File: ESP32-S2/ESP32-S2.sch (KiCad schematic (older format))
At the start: 45 parts, among them IC1 IP4220CZ6, J1 USB_A, J2 TYPE-C-31-M-12, J3 Conn_01x18_Male, J4 S2B-PH-SM4-TB(LF)(SN), J5 Conn_01x22_Male, SW1 SW_Push, SW2 SW_Push, U1 ESP32-S2-WROOM-ESP32-S2-WROOM, U2 MMBT8050, U3 MMBT8050, U4 MCP73831-2-OT, U5 AMS1117-3.3, U6 CH340C

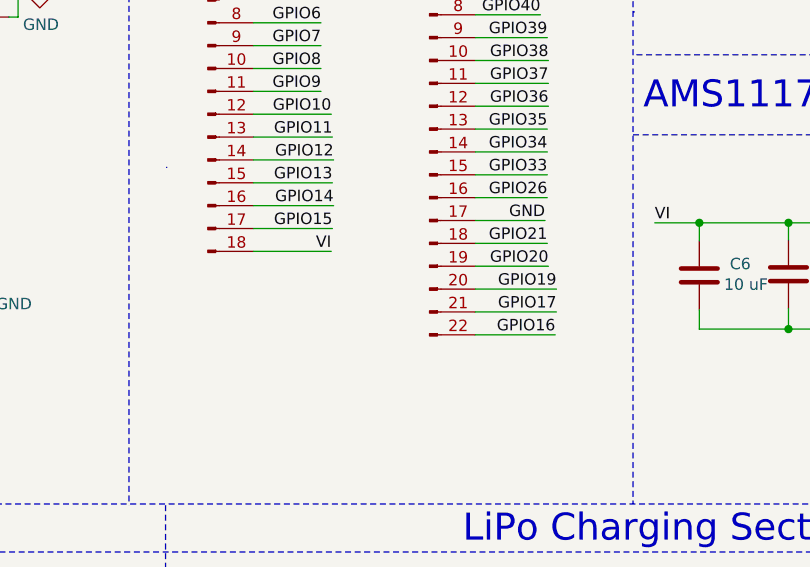
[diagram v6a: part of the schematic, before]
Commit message: Optimised 4-lyr routing v.4lyr.2
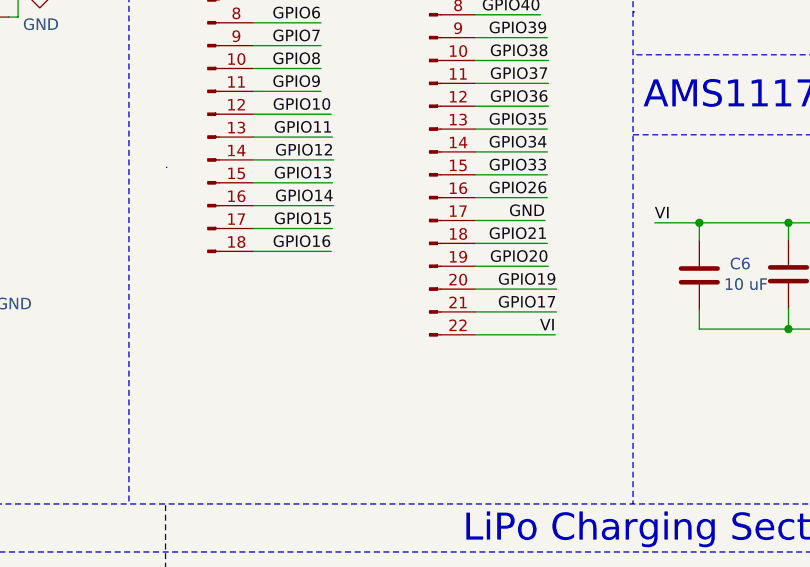
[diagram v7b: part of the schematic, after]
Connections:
- net GPIO16: now also J3.18 (Pin_18); no longer J5.22 (Pin_22)
- net VI: now also J5.22 (Pin_22); no longer J3.18 (Pin_18)
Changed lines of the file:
@@
 GPIO17
 Text Label 6225 3115 2    50   ~ 0
-GPIO16
+VI
 Wire Wire Line
 	5875 3015 6230 3015
@@
 $EndComp
 Text Label 5245 2750 2    50   ~ 0
-VI
+GPIO16
 Wire Wire Line
 	4905 2750 5245 2750

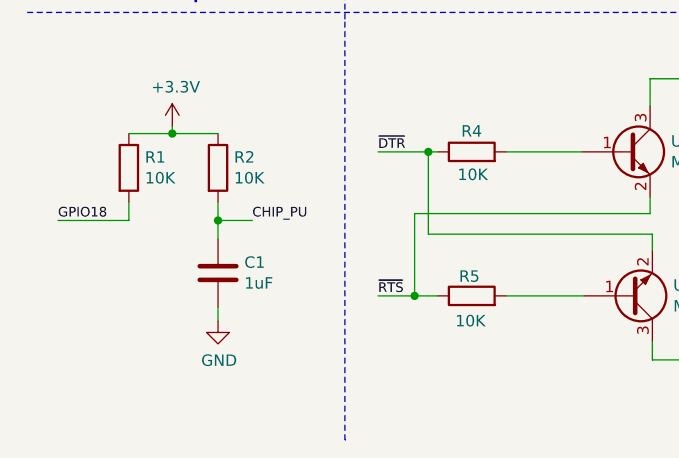
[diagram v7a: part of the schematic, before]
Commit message: Silkscreen Optimizations
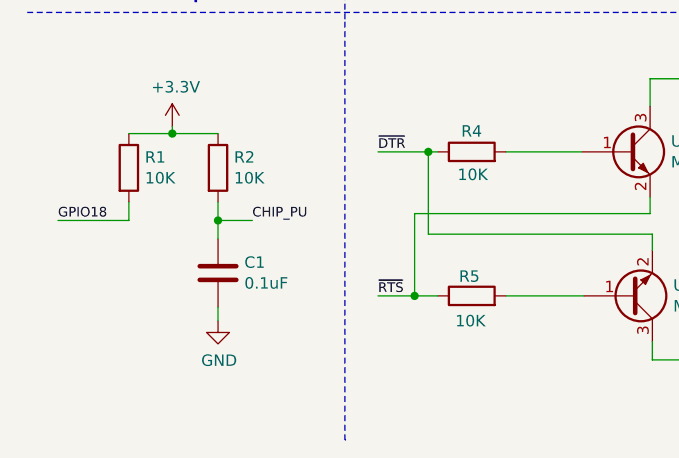
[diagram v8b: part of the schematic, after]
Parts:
- C1: value 1uF -> 0.1uF
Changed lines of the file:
@@
 P 1305 7070
 F 0 "C1" H 1420 7116 50  0000 L CNN
-F 1 "1uF" H 1420 7025 50  0000 L CNN
+F 1 "0.1uF" H 1420 7025 50  0000 L CNN
 F 2 "Capacitor_SMD:C_0603_1608Metric" H 1343 6920 50  0001 C CNN
 F 3 "~" H 1305 7070 50  0001 C CNN
